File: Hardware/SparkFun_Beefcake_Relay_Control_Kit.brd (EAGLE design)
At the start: 58.4 x 27.9 mm, 17 parts, among them Q2 2N3904, U6 RELAYPTH3

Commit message: Design ready for proto 1 review
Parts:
- removed FRAME1: FRAME-LETTER, SparkFun-Aesthetics:CREATIVE_COMMONS
- removed JP3: Load, SparkFun:SCREWTERMINAL-5MM-2
- removed R1: 10K, SparkFun:AXIAL-0.3
- removed U$1: LOGO-SFENEW, SparkFun:SFE-NEW-WEBLOGO
- added D2: BZT52, SparkFun-DiscreteSemi:DIODE-BZT52
- added FRAME2: FRAME-LETTER, SparkFun-Aesthetics:CREATIVE_COMMONS
- added JP1: (no value), SparkFun-Connectors:SCREWTERMINAL-5MM-3
- added LOGO1: SFE_LOGO_NAME_FLAME.2_INCH, SparkFun-Aesthetics:SFE_LOGO_NAME_FLAME_.2
- D1: device SparkFun:DIODE-1N4148 -> SparkFun-DiscreteSemi:DIODE-1N4148
- JP2: device SparkFun:SCREWTERMINAL-3.5MM-3 -> SparkFun-Connectors:SCREWTERMINAL-3.5MM-3
- LED1: device SparkFun:LED5MM -> SparkFun-LED:LED5MM
- Q2: device SparkFun:TO-92 -> SparkFun-DiscreteSemi:TO-92
- R2, R4: device SparkFun:AXIAL-0.3 -> SparkFun-Resistors:AXIAL-0.3
- U6: value RELAYPTH3 -> JQX-15F; device SparkFun:RELAY-T9A-2 -> SparkFun-Electromechanical:RELAY-T90
- moved U$11 33.1 mm to (39.4, 0.95)
- moved U$12 27.2 mm to (51.8, 26.7)
- moved D1 19.6 mm to (47.9, 1.27), turned to 180 degrees
- moved U6 16.7 mm to (39.4, 24.4), turned to 0 degrees
- moved R4 16.3 mm to (51.1, 23.2), turned to 0 degrees
- moved LED1 15.0 mm to (49.8, 18.7), turned to 90 degrees
- moved R2 10.7 mm to (52.4, 10.5)
- moved U$7 5.68 mm to (7.62, 27.9)
- moved U$3 5.08 mm to (7.62, 2.54)
- moved JP2 4.93 mm to (58.1, 11.8)
- moved U$5 3.59 mm to (58.4, 27.9)
- moved Q2 2.56 mm to (48.3, 10.5), turned to 270 degrees
- moved U$4 2.54 mm to (58.4, 2.54)
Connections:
- removed net LOAD1: JP3.2, U6.MAIN
- removed net LOAD2: JP3.1, U6.NO
- new net COMMON: JP1.3, U6.MAIN
- new net NC: JP1.1, U6.NC
- new net NO: JP1.2, U6.NO
- net COIL: now also D2.A, D2.C
- net GND: no longer R1.P$2
- net N$6: no longer R1.P$1
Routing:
- net COIL: track 18.5 -> 47.1 mm
- net RAW: track 64.7 -> 36.8 mm
- net LOAD1: track 22.0 -> 0.00 mm, vias 1 -> 0
- net LOAD2: track 19.1 -> 0.00 mm
- net GND: track 21.7 -> 10.9 mm
- net RELAY: track 13.8 -> 6.14 mm
- net N$6: track 13.5 -> 5.85 mm
- net N$9: track 4.34 -> 7.33 mm
- added copper zone on layer 1, net COMMON
- added copper zone on layer 16, net COMMON
- added copper zone on layer 1, net NC
- added copper zone on layer 16, net NC
- added copper zone on layer 1, net NO
- added copper zone on layer 16, net NO
- removed copper zone on layer 1, net LOAD1
- removed copper zone on layer 16, net LOAD1
- removed copper zone on layer 1, net LOAD2
- removed copper zone on layer 16, net LOAD2
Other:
- board size 58.4 x 27.9 mm -> 62.2 x 30.5 mm
- board text added: "Beefcake"
- board text added: "Beefcake Relay Control"
- board text added: "COM"
- board text added: "CUT FOR ZENER USE"
- board text added: "HIGH VOLTAGE"
- board text added: "JQX-15F 005-1Z1"
- board text added: "LOW VOLTAGE"
- board text added: "NC"
- board text added: "NO"
- board text added: "Units in inches"
- board text added: "v18"
- board text removed: "LOAD"
- board text removed: "Normally"
- board text removed: "Open"
- board text removed: "Relay Control PCB"
- board text removed: "T9A-30A/120V"
- board text removed: "v17"

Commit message: Running through review changes
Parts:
- added JP3: JUMPER-PAD-2-NC_BY_TRACE, SparkFun-Passives:PAD-JUMPER-2-NC_BY_TRACE_YES_SILK
- D1: device SparkFun-DiscreteSemi:DIODE-1N4148 -> SparkFun-DiscreteSemi:DIODE-1N4148-KIT
- D2: device SparkFun-DiscreteSemi:DIODE-BZT52 -> SparkFun-DiscreteSemi:DIODE-1N4148-KIT
- LED1: device SparkFun-LED:LED5MM -> SparkFun-LED:LED5MM-KIT
- LOGO1: value SFE_LOGO_NAME_FLAME.2_INCH -> SFE_LOGO_NAME_FLAME.1_INCH; device SparkFun-Aesthetics:SFE_LOGO_NAME_FLAME_.2 -> SparkFun-Aesthetics:SFE_LOGO_NAME_FLAME_.1
- Q2: device SparkFun-DiscreteSemi:TO-92 -> SparkFun-DiscreteSemi:TO-92-EZ
- R2, R4: value 1K -> 1k; device SparkFun-Resistors:AXIAL-0.3 -> SparkFun-Resistors:AXIAL-0.3EZ
- moved LOGO1 14.8 mm to (25.0, 2.86)
- moved FRAME2 4.49 mm to (-1.14, -13.1)
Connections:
- net COIL: now also JP3.1, JP3.2
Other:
- board text added: "Both layers to be 2 OZ copper"
- board text added: "Component Side"
- board text added: "N. Seidle/M. Taylor"
- board text added: "v20"
- board text removed: "N. Seidle/Joel Bartlett"
- board text removed: "v18"

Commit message: Ready for QC's review
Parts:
- R2, R4: value 1k -> 1K
- moved U$11 27.4 mm to (50.5, 26.0)
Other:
- board text added: "Beefcake Ctrl"
- board text added: "CAUTION: RISK OF ELECTRIC SHOCK!"
- board text added: "Solder Side"
- board text removed: "Beefcake"

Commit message: updated bom
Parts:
- removed JP3: JUMPER-PAD-2-NC_BY_TRACE, SparkFun-Passives:PAD-JUMPER-2-NC_BY_TRACE_YES_SILK
- added J1: (no value), SparkFun-Connectors:SCREWTERMINAL-5MM-3
- JP1: value (none) -> JUMPER-PAD-2-NC_BY_TRACE; device SparkFun-Connectors:SCREWTERMINAL-5MM-3 -> SparkFun-Passives:PAD-JUMPER-2-NC_BY_TRACE_YES_SILK
- moved JP1 43.4 mm to (47.9, 3.49), flipped to the bottom, turned to 0 degrees
- renumbered JP2 to J2, U6 to K1
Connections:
- net COIL: now also JP1.1, JP1.2; no longer JP3.1, JP3.2
- net COMMON: now also J1.3; no longer JP1.3
- net NC: now also J1.1; no longer JP1.1
- net NO: now also J1.2; no longer JP1.2
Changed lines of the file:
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@@
 <layer number="17" name="Pads" color="2" fill="1" visible="yes" active="yes"/>
 <layer number="18" name="Vias" color="2" fill="1" visible="yes" active="yes"/>
-<layer number="19" name="Unrouted" color="6" fill="1" visible="no" active="yes"/>
+<layer number="19" name="Unrouted" color="6" fill="1" visible="yes" active="yes"/>
 <layer number="20" name="Dimension" color="15" fill="1" visible="yes" active="yes"/>
 <layer number="21" name="tPlace" color="16" fill="1" visible="yes" active="yes"/>
 <layer number="22" name="bPlace" color="14" fill="1" visible="yes" active="yes"/>
-<layer number="23" name="tOrigins" color="15" fill="1" visible="no" active="yes"/>
-<layer number="24" name="bOrigins" color="15" fill="1" visible="no" active="yes"/>
+<layer number="23" name="tOrigins" color="15" fill="1" visible="yes" active="yes"/>
+<layer number="24" name="bOrigins" color="15" fill="1" visible="yes" active="yes"/>
 <layer number="25" name="tNames" color="7" fill="1" visible="no" active="yes"/>
 <layer number="26" name="bNames" color="7" fill="1" visible="no" active="yes"/>
@@
 <layer number="37" name="tTest" color="7" fill="1" visible="no" active="yes"/>
 <layer number="38" name="bTest" color="7" fill="1" visible="no" active="yes"/>
-<layer number="39" name="tKeepout" color="4" fill="11" visible="yes" active="yes"/>
-<layer number="40" name="bKeepout" color="1" fill="11" visible="yes" active="yes"/>
+<layer number="39" name="tKeepout" color="4" fill="11" visible="no" active="yes"/>
+<layer number="40" name="bKeepout" color="1" fill="11" visible="no" active="yes"/>
 <layer number="41" name="tRestrict" color="4" fill="10" visible="no" active="yes"/>
 <layer number="42" name="bRestrict" color="1" fill="10" visible="no" active="yes"/>
 <layer number="43" name="vRestrict" color="2" fill="10" visible="no" active="yes"/>
 <layer number="44" name="Drills" color="7" fill="1" visible="no" active="yes"/>
-<layer number="45" name="Holes" color="7" fill="1" visible="no" active="yes"/>
+<layer number="45" name="Holes" color="7" fill="1" visible="yes" active="yes"/>
 <layer number="46" name="Milling" color="3" fill="1" visible="no" active="yes"/>
-<layer number="47" name="Measures" color="7" fill="1" visible="yes" active="yes"/>
+<layer number="47" name="Measures" color="7" fill="1" visible="no" active="yes"/>
 <layer number="48" name="Document" color="7" fill="1" visible="no" active="yes"/>
 <layer number="49" name="Reference" color="7" fill="1" visible="no" active="yes"/>
 <layer number="50" name="dxf" color="7" fill="1" visible="no" active="yes"/>
-<layer number="51" name="tDocu" color="6" fill="1" visible="no" active="yes"/>
+<layer number="51" name="tDocu" color="6" fill="1" visible="yes" active="yes"/>
 <layer number="52" name="bDocu" color="7" fill="1" visible="no" active="yes"/>
 <layer number="53" name="tGND_GNDA" color="7" fill="9" visible="no" active="no"/>
@@
 <attribute name="PROD_ID" value="DIO-08378" x="47.9425" y="1.27" size="1.778" layer="27" rot="R180" display="off"/>
 </element>
-<element name="JP2" library="SparkFun-Connectors" package="SCREWTERMINAL-3.5MM-3" value="" x="58.1025" y="11.811" smashed="yes" rot="R90">
+<element name="J2" library="SparkFun-Connectors" package="SCREWTERMINAL-3.5MM-3" value="" x="58.1025" y="11.811" smashed="yes" rot="R90">
 <attribute name="PROD_ID" value="CONN-08288" x="58.1025" y="11.811" size="1.778" layer="27" rot="R90" display="off"/>
 <attribute name="NAME" x="58.039" y="21.2725" size="0.8128" layer="25" font="vector" ratio="15" rot="R180" align="center"/>
 <attribute name="VALUE" x="56.8325" y="10.541" size="0.4064" layer="27" rot="R90"/>
 </element>
-<element name="U6" library="SparkFun-Electromechanical" package="RELAY-T90" value="JQX-15F" x="39.37" y="24.4475">
+<element name="K1" library="SparkFun-Electromechanical" package="RELAY-T90" value="JQX-15F" x="39.37" y="24.4475">
 <attribute name="PROD_ID" value="COMP-10736" x="39.37" y="24.4475" size="1.778" layer="27" display="off"/>
 <attribute name="VALUE" value="JQX-15F" x="39.37" y="24.4475" size="1.778" layer="27" display="off"/>
@@
 <element name="U$11" library="SparkFun" package="SFE-LOGO-FLAME" value="" x="50.4825" y="26.035"/>
 <element name="U$12" library="SparkFun" package="OSHW-LOGO-S" value="OSHW-LOGOS" x="51.7525" y="26.67" rot="MR0"/>
-<element name="JP1" library="SparkFun-Connectors" package="SCREWTERMINAL-5MM-3" value="" x="7.9375" y="20.2438" smashed="yes" rot="R270">
+<element name="J1" library="SparkFun-Connectors" package="SCREWTERMINAL-5MM-3" value="" x="7.9375" y="20.2438" smashed="yes" rot="R270">
 <attribute name="STOREFRONT_ID" value="PRT-08433" x="7.9375" y="20.2438" size="1.778" layer="27" rot="R270" display="off"/>
 <attribute name="NAME" x="12.9413" y="24.4475" size="0.8128" layer="25" font="vector" ratio="15" rot="R180"/>
 <attribute name="VALUE" x="9.2075" y="21.5138" size="0.4064" layer="27" rot="R270"/>
+<attribute name="PROD_ID" value="CONN-10134" x="7.9375" y="20.2438" size="1.778" layer="27" rot="R270" display="off"/>
 </element>
 <element name="D2" library="SparkFun-DiscreteSemi" package="DIODE-1N4148-KIT" value="BZT52" x="47.9425" y="3.4925" smashed="yes">
@@
 <element name="FRAME2" library="SparkFun-Aesthetics" package="CREATIVE_COMMONS" value="FRAME-LETTER" x="-1.143" y="-13.081"/>
 <element name="LOGO1" library="SparkFun-Aesthetics" package="SFE_LOGO_NAME_FLAME_.1" value="SFE_LOGO_NAME_FLAME.1_INCH" x="24.9555" y="2.8575" rot="MR0"/>
-<element name="JP3" library="SparkFun-Passives" package="PAD-JUMPER-2-NC_BY_TRACE_YES_SILK" value="JUMPER-PAD-2-NC_BY_TRACE" x="47.9425" y="3.4925" rot="MR0"/>
+<element name="JP1" library="SparkFun-Passives" package="PAD-JUMPER-2-NC_BY_TRACE_YES_SILK" value="JUMPER-PAD-2-NC_BY_TRACE" x="47.9425" y="3.4925" rot="MR0"/>
 </elements>
 <signals>
 <signal name="GND">
 <contactref element="Q2" pad="1"/>
-<contactref element="JP2" pad="1"/>
+<contactref element="J2" pad="1"/>
 <wire x1="48.26" y1="11.7475" x2="49.2125" y2="12.7" width="0.4064" layer="1"/>
 <wire x1="49.2125" y1="12.7" x2="50.8" y2="12.7" width="0.4064" layer="1"/>
@@
 <contactref element="D1" pad="C"/>
 <contactref element="LED1" pad="A"/>
-<contactref element="JP2" pad="3"/>
-<contactref element="U6" pad="COIL1"/>
+<contactref element="J2" pad="3"/>
+<contactref element="K1" pad="COIL1"/>
 <wire x1="44.1325" y1="1.27" x2="42.545" y2="1.27" width="0.4064" layer="1"/>
 <wire x1="42.545" y1="1.27" x2="41.91" y2="1.905" width="0.4064" layer="1"/>
@@
 <signal name="RELAY">
 <contactref element="R2" pad="P$2"/>
-<contactref element="JP2" pad="2"/>
+<contactref element="J2" pad="2"/>
 <wire x1="58.1025" y1="15.311" x2="53.411" y2="15.311" width="0.4064" layer="1"/>
 <wire x1="53.411" y1="15.311" x2="52.3875" y2="14.2875" width="0.4064" layer="1"/>
@@
 <contactref element="Q2" pad="3"/>
 <contactref element="R4" pad="P$1"/>
-<contactref element="U6" pad="COIL2"/>
+<contactref element="K1" pad="COIL2"/>
 <contactref element="D2" pad="C"/>
 <wire x1="48.26" y1="9.2075" x2="48.26" y2="6.985" width="0.4064" layer="1"/>
@@
 <wire x1="47.625" y1="6.35" x2="44.7675" y2="6.35" width="0.4064" layer="1"/>
 <wire x1="44.7675" y1="6.35" x2="44.1325" y2="5.715" width="0.4064" layer="1"/>
-<contactref element="JP3" pad="1"/>
+<contactref element="JP1" pad="1"/>
 <wire x1="44.1325" y1="5.715" x2="44.1325" y2="3.4925" width="0.4064" layer="1"/>
 <contactref element="D1" pad="A"/>
 <contactref element="D2" pad="A"/>
-<contactref element="JP3" pad="2"/>
+<contactref element="JP1" pad="2"/>
 <wire x1="51.7525" y1="1.27" x2="51.7525" y2="3.4925" width="0.4064" layer="16"/>
 <wire x1="51.7525" y1="3.4925" x2="48.4505" y2="3.4925" width="0.4064" layer="16"/>
@@
 <vertex x="12.7" y="5.715"/>
 </polygon>
-<contactref element="JP1" pad="3"/>
-<contactref element="U6" pad="MAIN"/>
+<contactref element="J1" pad="3"/>
+<contactref element="K1" pad="MAIN"/>
 <polygon width="0.254" layer="16" isolate="0.3048" thermals="no">
 <vertex x="14.605" y="3.81"/>
@@
 <via x="1.27" y="21.2725" extent="1-16" drill="0.508"/>
 <via x="3.81" y="21.2725" extent="1-16" drill="0.508"/>
-<contactref element="JP1" pad="1"/>
+<contactref element="J1" pad="1"/>
 <polygon width="0.254" layer="1" isolate="0.3048" thermals="no">
 <vertex x="18.7325" y="26.3525"/>
@@
 <vertex x="18.415" y="26.67"/>
 </polygon>
-<contactref element="U6" pad="NC"/>
+<contactref element="K1" pad="NC"/>
 <polygon width="0.254" layer="16" isolate="0.3048" thermals="no">
 <vertex x="18.7325" y="26.3525"/>
@@
 <vertex x="21.9075" y="26.035"/>
 </polygon>
-<contactref element="JP1" pad="2"/>
-<contactref element="U6" pad="NO"/>
+<contactref element="J1" pad="2"/>
+<contactref element="K1" pad="NO"/>
 <polygon width="0.254" layer="16" isolate="0.3048" thermals="no">
 <vertex x="22.479" y="26.6065"/>

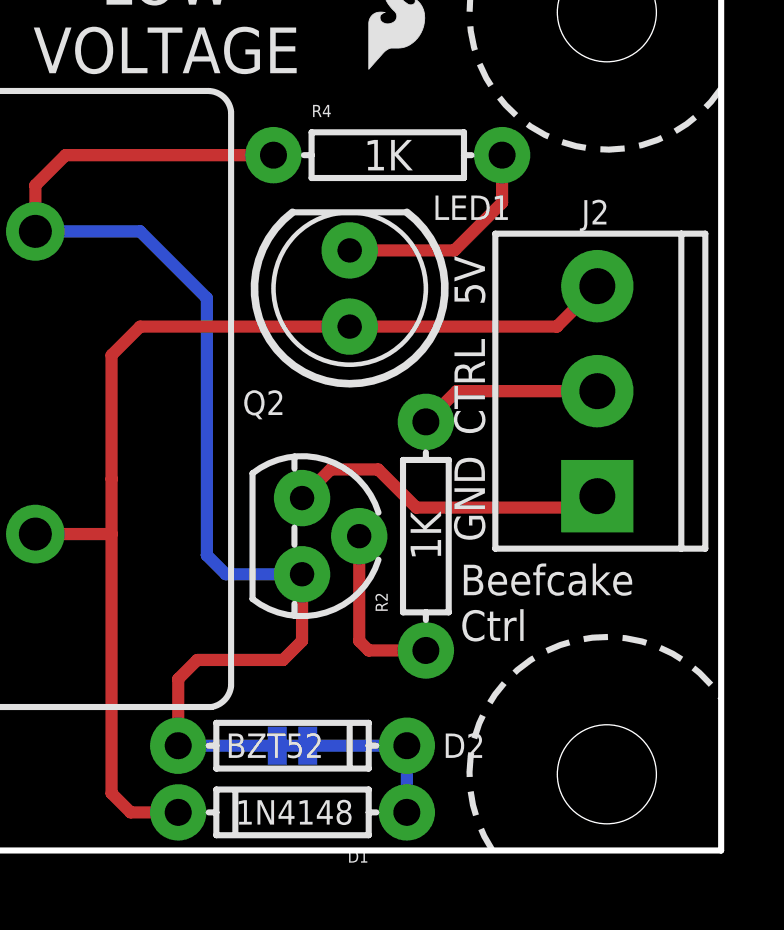
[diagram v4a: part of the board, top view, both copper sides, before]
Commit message: updated silk for redboard review
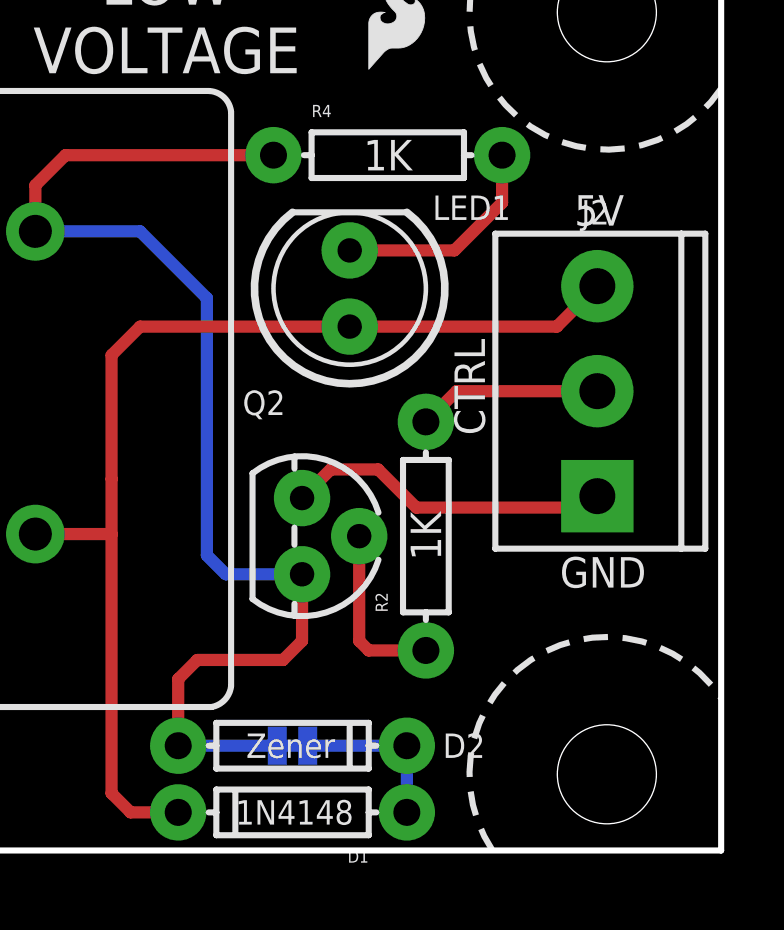
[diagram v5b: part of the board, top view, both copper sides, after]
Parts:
- D2: value BZT52 -> Zener
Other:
- board text removed: "Beefcake Ctrl"

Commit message: Finished for reds review, implemented changes
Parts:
- D2: device SparkFun-DiscreteSemi:DIODE-1N4148-KIT -> SparkFun-DiscreteSemi:DIODE-BZT52
- JP1: value JUMPER-PAD-2-NC_BY_TRACE -> JUMPER-PAD-2-NOYES_SILK; device SparkFun-Passives:PAD-JUMPER-2-NC_BY_TRACE_YES_SILK -> SparkFun-Passives:PAD-JUMPER-2-NO_YES_SILK
- turned D2 to 180 degrees
- turned JP1 to 180 degrees
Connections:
- net RAW renamed VCC
- new net DIODENODE: D1.A, D2.A, JP1.2
- net COIL: no longer D1.A, D2.A, JP1.2
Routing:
- net COIL: track 47.5 -> 41.0 mm
- net DIODENODE: track 0.00 -> 5.58 mm
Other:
- outline, holes or cut-outs redrawn
- board text added: "5V current: 150mA CTRL current: 5mA"
- board text added: "CAUTION:"
- board text added: "RISK OF ELECTRIC SHOCK!"
- board text added: "SHORT FOR ZENER BYPASS"
- board text removed: "CAUTION: RISK OF ELECTRIC SHOCK!"
- board text removed: "CUT FOR ZENER USE"

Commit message: prepping for QC action
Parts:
- D2: device SparkFun-DiscreteSemi:DIODE-BZT52 -> SparkFun-DiscreteSemi:DIODE-1N4148-KIT
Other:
- board text added: "BRIDGE FOR ZENER BYPASS"
- board text removed: "SHORT FOR ZENER BYPASS"
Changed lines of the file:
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@@
 <layer number="14" name="Route14" color="1" fill="6" visible="no" active="no"/>
 <layer number="15" name="Route15" color="4" fill="6" visible="no" active="no"/>
-<layer number="16" name="Bottom" color="1" fill="1" visible="no" active="yes"/>
+<layer number="16" name="Bottom" color="1" fill="1" visible="yes" active="yes"/>
 <layer number="17" name="Pads" color="2" fill="1" visible="yes" active="yes"/>
 <layer number="18" name="Vias" color="2" fill="1" visible="yes" active="yes"/>
@@
 <layer number="20" name="Dimension" color="15" fill="1" visible="yes" active="yes"/>
 <layer number="21" name="tPlace" color="16" fill="1" visible="yes" active="yes"/>
-<layer number="22" name="bPlace" color="14" fill="1" visible="no" active="yes"/>
-<layer number="23" name="tOrigins" color="15" fill="1" visible="yes" active="yes"/>
+<layer number="22" name="bPlace" color="14" fill="1" visible="yes" active="yes"/>
+<layer number="23" name="tOrigins" color="15" fill="1" visible="no" active="yes"/>
 <layer number="24" name="bOrigins" color="15" fill="1" visible="no" active="yes"/>
 <layer number="25" name="tNames" color="7" fill="1" visible="no" active="yes"/>
@@
 <layer number="28" name="bValues" color="7" fill="1" visible="no" active="yes"/>
 <layer number="29" name="tStop" color="7" fill="3" visible="no" active="yes"/>
-<layer number="30" name="bStop" color="7" fill="6" visible="no" active="yes"/>
+<layer number="30" name="bStop" color="7" fill="6" visible="yes" active="yes"/>
 <layer number="31" name="tCream" color="7" fill="4" visible="no" active="yes"/>
 <layer number="32" name="bCream" color="7" fill="5" visible="no" active="yes"/>
@@
 <layer number="49" name="Reference" color="7" fill="1" visible="no" active="yes"/>
 <layer number="50" name="dxf" color="7" fill="1" visible="no" active="yes"/>
-<layer number="51" name="tDocu" color="6" fill="1" visible="no" active="yes"/>
+<layer number="51" name="tDocu" color="6" fill="1" visible="yes" active="yes"/>
 <layer number="52" name="bDocu" color="7" fill="1" visible="no" active="yes"/>
 <layer number="53" name="tGND_GNDA" color="7" fill="9" visible="no" active="no"/>
@@
 <circle x="58.42" y="2.54" radius="4.572" width="0.254" layer="41"/>
 <circle x="7.62" y="2.54" radius="4.572" width="0.254" layer="41"/>
-<text x="45.593" y="7.239" size="1.016" layer="22" font="vector" ratio="15" rot="MR90" align="center-left">SHORT FOR
+<text x="45.593" y="7.239" size="1.016" layer="22" font="vector" ratio="15" rot="MR90" align="center-left">BRIDGE FOR
 ZENER BYPASS</text>
 <wire x1="47.9425" y1="5.3975" x2="47.9425" y2="6.35" width="0.2032" layer="22"/>
@@
 <element name="LOGO1" library="SparkFun-Aesthetics" package="SFE_LOGO_NAME_FLAME_.1" value="SFE_LOGO_NAME_FLAME.1_INCH" x="24.9555" y="2.8575" rot="MR0"/>
 <element name="JP1" library="SparkFun-Passives" package="PAD-JUMPER-2-NO_YES_SILK" value="JUMPER-PAD-2-NOYES_SILK" x="47.9425" y="3.4925" rot="MR180"/>
-<element name="D2" library="SparkFun-DiscreteSemi" package="DIODE-BZT52" value="Zener" x="47.9425" y="3.4925" rot="R180">
-<attribute name="PROD-ID" value="DIO-08199" x="47.9425" y="3.4925" size="1.778" layer="27" font="vector" ratio="15" rot="R180" display="off"/>
+<element name="D2" library="SparkFun-DiscreteSemi" package="DIODE-1N4148-KIT" value="Zener" x="47.9425" y="3.4925" smashed="yes" rot="R180">
+<attribute name="PROD_ID" value="Generic" x="47.9425" y="3.4925" size="1.778" layer="27" rot="R180" display="off"/>
+<attribute name="NAME" x="50.4825" y="2.2225" size="0.4064" layer="25" rot="R180"/>
+<attribute name="VALUE" x="49.9745" y="4.0005" size="0.8128" layer="21" font="vector" ratio="15" rot="R180"/>
 </element>
 </elements>
